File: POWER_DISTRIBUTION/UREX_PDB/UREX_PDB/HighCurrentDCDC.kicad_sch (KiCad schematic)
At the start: 23 parts, among them U5 XTPS552892RYQR

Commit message: V1 Full Fabrication(Freezed design)
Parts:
- C20: value 18nF -> 22nF
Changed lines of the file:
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@@
 			)
 		)
-		(property "Value" "18nF"
+		(property "Value" "22nF"
 			(at 156.21 133.604 0)
 			(show_name no)

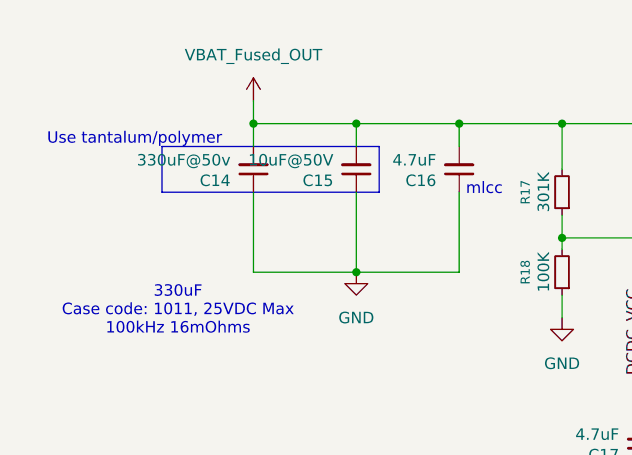
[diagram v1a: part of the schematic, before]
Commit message: fixed jarring pcb issues
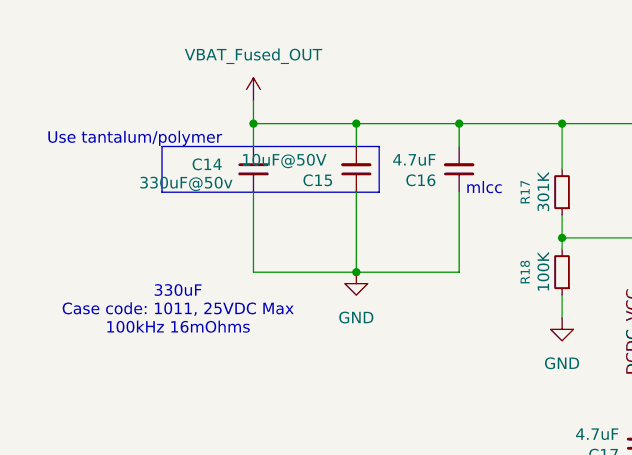
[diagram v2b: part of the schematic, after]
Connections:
- net GND: now also C14.2; no longer C14.1
- net VBAT_Fused_OUT: now also C14.1; no longer C14.2
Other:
- moved on the sheet: C14
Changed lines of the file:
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@@
 		)
 		(property "Value" "10uF@50V"
-			(at 49.53 86.614 0)
+			(at 48.768 86.614 0)
 			(show_name no)
 			(do_not_autoplace no)
@@
 	(symbol
 		(lib_id "Device:C_Small")
-		(at 40.64 87.63 180)
+		(at 40.64 87.63 0)
 		(unit 1)
 		(body_style 1)
@@
 		(dnp no)
 		(property "Reference" "C14"
-			(at 38.1 88.8938 0)
+			(at 33.782 87.122 0)
 			(show_name no)
 			(do_not_autoplace no)
@@
 		)
 		(property "Value" "330uF@50v"
-			(at 38.1 86.614 0)
+			(at 27.94 89.154 0)
 			(show_name no)
 			(do_not_autoplace no)
